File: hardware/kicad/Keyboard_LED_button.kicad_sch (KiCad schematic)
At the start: 26 parts, among them J1 JST 4 Pin Qwiic I2C Connector, J2 JST 4 Pin Qwiic I2C Connector, J3 Castellated_Edge_4pin_Qwiic_S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, J4 Castellated_Edge_5pin_Firmware, SW1 SW_Push, U1 CH32V003F4U6, U2 MT3540‑F23

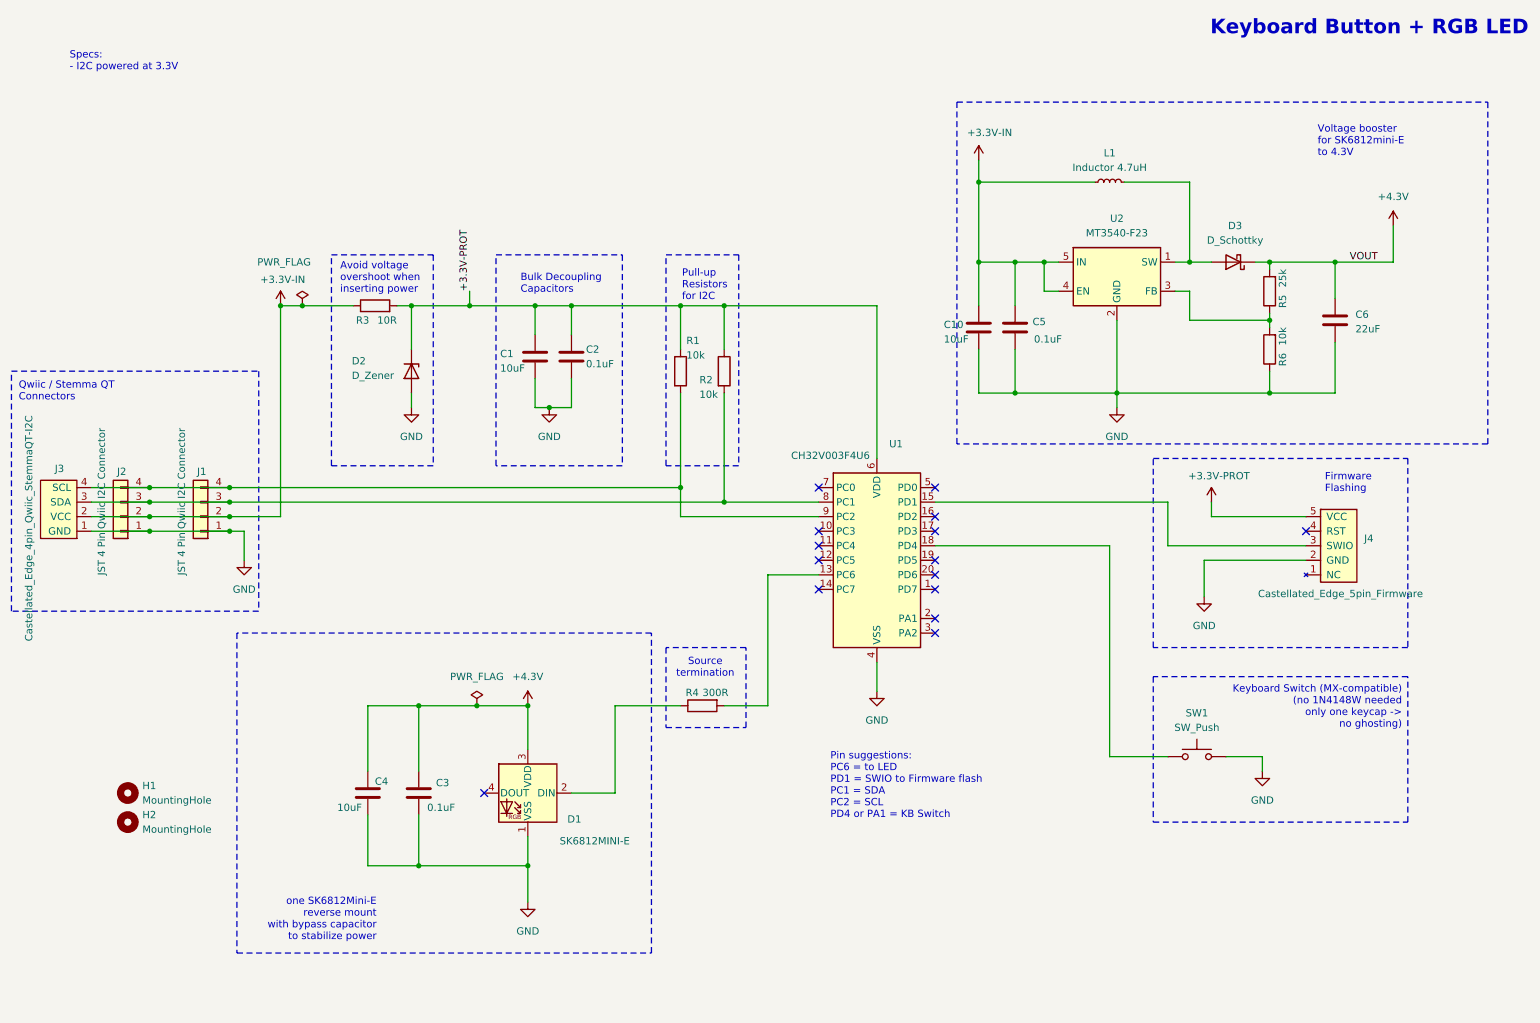
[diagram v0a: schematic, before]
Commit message: LED Button V2 hardware: updated KiCad schematic + PCB; add V2 + V1.1 schematic PDFs
Updated Keyboard_LED_button KiCad project (schematic + board) for v2.0; added
Schematics_LEDButton_V2_20260616.pdf and renamed-as Schematics_LEDButton_V1_1_20260408.pdf;
removed obsolete Schematics_Keyboard_Button_20260408.pdf and .keep placeholders.
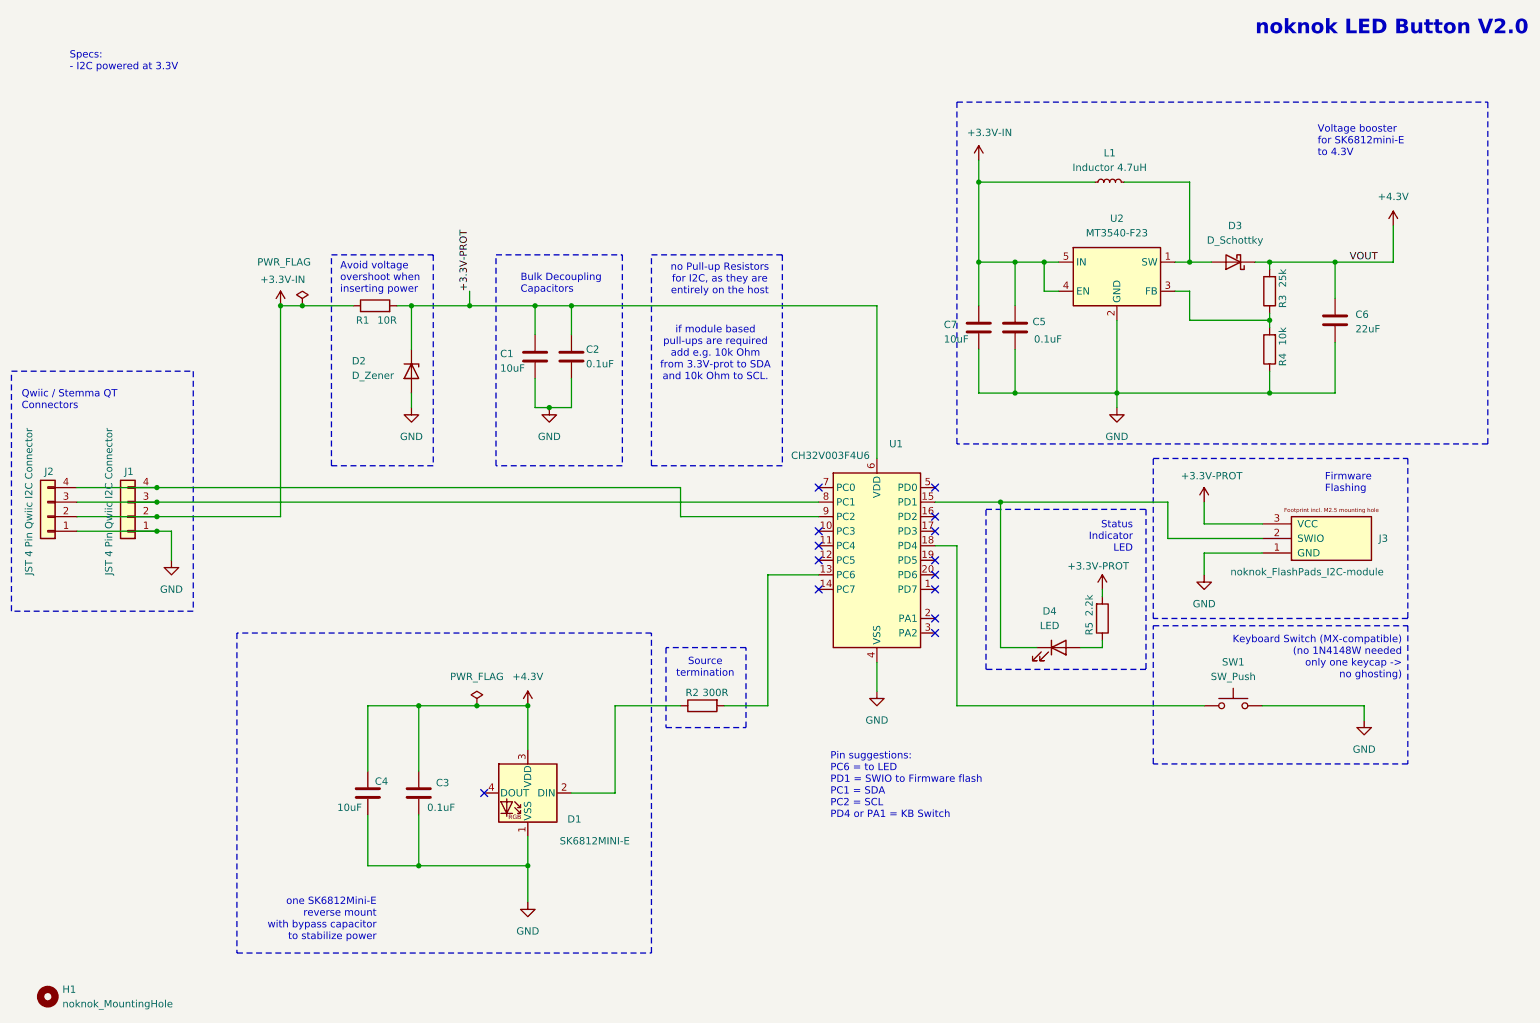
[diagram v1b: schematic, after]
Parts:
- removed H1, H2: MountingHole, MountingHole:MountingHole_2.2mm_M2, symbol Mechanical:MountingHole
- removed J3: Castellated_Edge_4pin_Qwiic_StemmaQT-I2C, Chris_Library:Castellated_edge_pad_I2C_4pin, symbol noknok_KiCad_Symbol_Library:Castellated_Edge_4pin_Qwiic_StemmaQT-I2C
- removed J4: Castellated_Edge_5pin_Firmware, Chris_Library:Castellated_edge_pad_Firmware, symbol noknok_KiCad_Symbol_Library:Castellated_Edge_5pin_Firmware
- removed R1, R2: 10k, Resistor_SMD:R_0603_1608Metric, symbol Device:R
- added D4: LED, LED_SMD:LED_0603_1608Metric, symbol Device:LED
- added H1: noknok_MountingHole, noknok:noknok_MountingHole_2.5mm_M2.5, symbol noknok:noknok_MountingHole
- added J3: noknok_FlashPads_I2C-module, noknok:noknok_FlashPads_I2C-module_1x3_M2.5, symbol noknok:noknok_FlashPads_I2C-module
- added R5: 2.2k, Resistor_SMD:R_0603_1608Metric, symbol Device:R
- renumbered C10 to C7, R3 to R1, R4 to R2, R5 to R3, R6 to R4
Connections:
- net +3.3V-PROT: now also J3.3 (VCC), R5.2
- net GND: now also J3.1 (GND)
- net at U1.15 (PD1): now also D4.1 (K), J3.2 (SWIO)
- new net: D4.2 (A), R5.1
- no-connect marks 15 -> 14
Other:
- note added: "Status Indicator LED"
- note added: "if module based pull-ups are required add e.g. 10k Ohm from 3.3V-prot to SDA and 10k Ohm to SCL."
- note added: "no Pull-up Resistors for I2C, as they are entirely on the host"
- note added: "noknok LED Button V2.0"
- note removed: "Keyboard Button + RGB LED"
- note removed: "Pull-up Resistors for I2C"
- title: Keyboard Button on CHV32003J4M6 -> LED Button on CHV32003J4M6
- moved on the sheet: J1, J2, SW1
